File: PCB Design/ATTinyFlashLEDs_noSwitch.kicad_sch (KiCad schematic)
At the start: 11 parts, among them J1 Conn_01x04_Pin, J2 Conn_01x04_Pin, J3 Conn_01x03_Pin, U1 ATtiny85V-10P

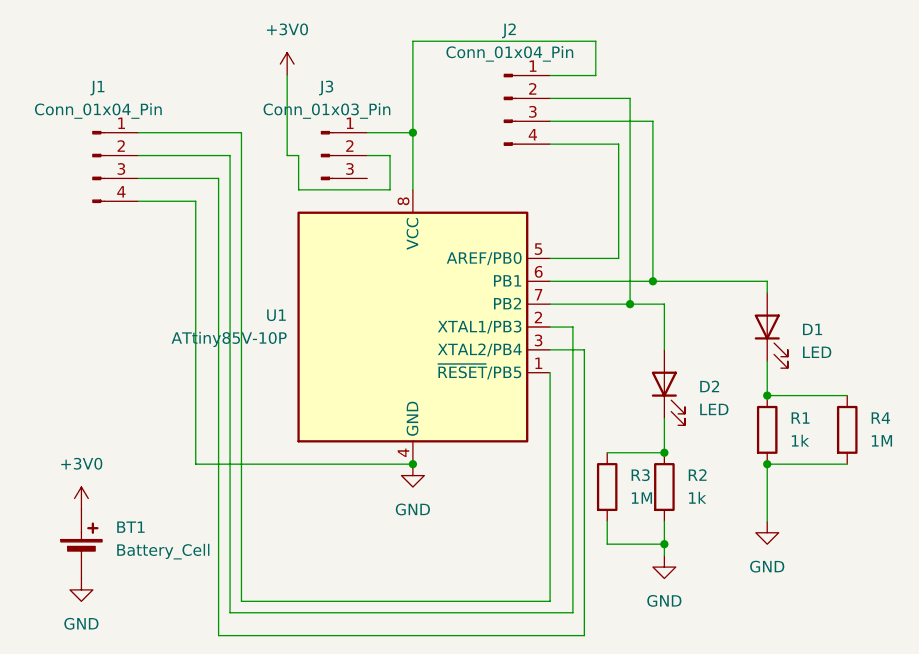
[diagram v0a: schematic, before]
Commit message: Added decoupling capacitor, moved power trace to back copper
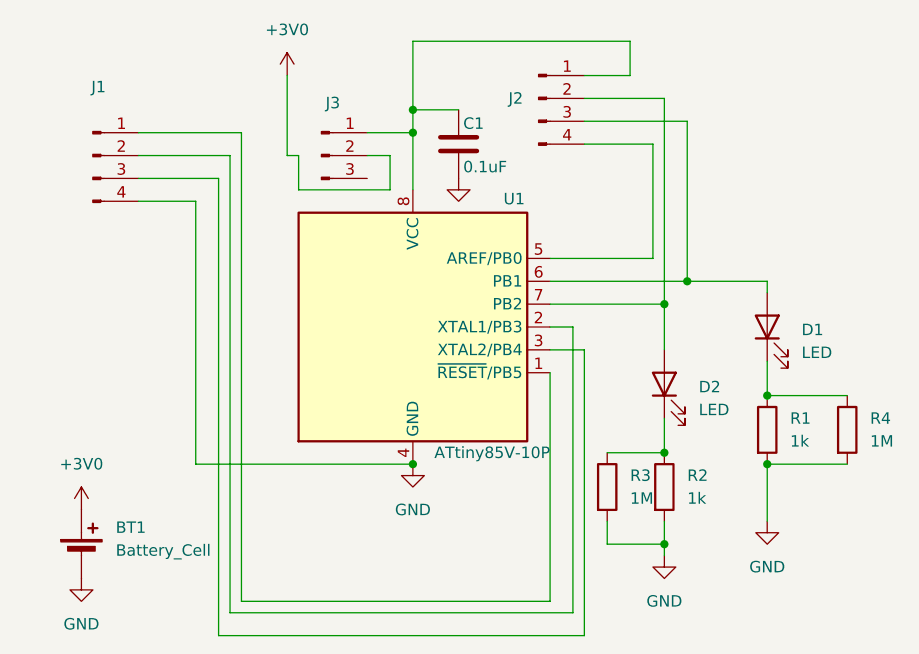
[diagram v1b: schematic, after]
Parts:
- added C1: 0.1uF, Capacitor_SMD:C_0603_1608Metric_Pad1.08x0.95mm_HandSolder, symbol Device:C
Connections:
- net GND: now also C1.2
- net at J2.1 (Pin_1), J3.1 (Pin_1), U1.8 (VCC): now also C1.1
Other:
- moved on the sheet: J2
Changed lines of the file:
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@@
 	)
 	(junction
-		(at 83.82 43.18)
+		(at 85.09 45.72)
+		(diameter 0)
+		(color 0 0 0 0)
+	)
+	(junction
+		(at 57.15 24.13)
 		(diameter 0)
 		(color 0 0 0 0)
@@
 	)
 	(junction
-		(at 81.28 45.72)
+		(at 57.15 26.67)
 		(diameter 0)
 		(color 0 0 0 0)
 	)
 	(junction
-		(at 57.15 26.67)
+		(at 87.63 43.18)
 		(diameter 0)
 		(color 0 0 0 0)
@@
 	(wire
 		(pts
-			(xy 81.28 22.86) (xy 81.28 45.72)
+			(xy 57.15 24.13) (xy 62.23 24.13)
+		)
+		(stroke
+			(width 0)
+			(type default)
+		)
+	)
+	(wire
+		(pts
+			(xy 85.09 22.86) (xy 85.09 45.72)
 		)
 		(stroke
@@
 	(wire
 		(pts
-			(xy 72.39 25.4) (xy 83.82 25.4)
+			(xy 76.2 25.4) (xy 87.63 25.4)
 		)
 		(stroke
@@
 	(wire
 		(pts
-			(xy 83.82 43.18) (xy 96.52 43.18)
-		)
-		(stroke
-			(width 0)
-			(type default)
-		)
-	)
-	(wire
-		(pts
-			(xy 81.28 45.72) (xy 85.09 45.72)
-		)
-		(stroke
-			(width 0)
-			(type default)
-		)
-	)
-	(wire
-		(pts
 			(xy 26.67 34.29) (xy 33.02 34.29)
 		)
@@
 	(wire
 		(pts
-			(xy 83.82 25.4) (xy 83.82 43.18)
+			(xy 87.63 25.4) (xy 87.63 43.18)
 		)
 		(stroke
@@
 	(wire
 		(pts
-			(xy 72.39 27.94) (xy 80.01 27.94)
+			(xy 76.2 27.94) (xy 83.82 27.94)
 		)
 		(stroke
@@
 	(wire
 		(pts
-			(xy 72.39 20.32) (xy 77.47 20.32)
-		)
-		(stroke
-			(width 0)
-			(type default)
-		)
-	)
-	(wire
-		(pts
-			(xy 77.47 16.51) (xy 57.15 16.51)
+			(xy 76.2 20.32) (xy 81.28 20.32)
+		)
+		(stroke
+			(width 0)
+			(type default)
+		)
+	)
+	(wire
+		(pts
+			(xy 57.15 24.13) (xy 57.15 26.67)
+		)
+		(stroke
+			(width 0)
+			(type default)
+		)
+	)
+	(wire
+		(pts
+			(xy 81.28 16.51) (xy 57.15 16.51)
 		)
 		(stroke
@@
 	(wire
 		(pts
-			(xy 72.39 40.64) (xy 80.01 40.64)
-		)
-		(stroke
-			(width 0)
-			(type default)
-		)
-	)
-	(wire
-		(pts
-			(xy 72.39 43.18) (xy 83.82 43.18)
+			(xy 72.39 40.64) (xy 83.82 40.64)
+		)
+		(stroke
+			(width 0)
+			(type default)
+		)
+	)
+	(wire
+		(pts
+			(xy 87.63 43.18) (xy 96.52 43.18)
+		)
+		(stroke
+			(width 0)
+			(type default)
+		)
+	)
+	(wire
+		(pts
+			(xy 72.39 43.18) (xy 87.63 43.18)
 		)
 		(stroke
@@
 	(wire
 		(pts
-			(xy 72.39 22.86) (xy 81.28 22.86)
+			(xy 76.2 22.86) (xy 85.09 22.86)
 		)
 		(stroke
@@
 	(wire
 		(pts
-			(xy 80.01 40.64) (xy 80.01 27.94)
-		)
-		(stroke
-			(width 0)
-			(type default)
-		)
-	)
-	(wire
-		(pts
-			(xy 57.15 16.51) (xy 57.15 26.67)
-		)
-		(stroke
-			(width 0)
-			(type default)
-		)
-	)
-	(wire
-		(pts
-			(xy 72.39 45.72) (xy 81.28 45.72)
+			(xy 83.82 40.64) (xy 83.82 27.94)
+		)
+		(stroke
+			(width 0)
+			(type default)
+		)
+	)
+	(wire
+		(pts
+			(xy 57.15 16.51) (xy 57.15 24.13)
+		)
+		(stroke
+			(width 0)
+			(type default)
+		)
+	)
+	(wire
+		(pts
+			(xy 72.39 45.72) (xy 85.09 45.72)
 		)
 		(stroke
@@
 	(wire
 		(pts
-			(xy 77.47 20.32) (xy 77.47 16.51)
+			(xy 81.28 20.32) (xy 81.28 16.51)
 		)
 		(stroke
@@
 	(symbol
 		(lib_id "Connector:Conn_01x04_Pin")
-		(at 67.31 22.86 0)
+		(at 71.12 22.86 0)
 		(unit 1)
 		(exclude_from_sim no)
@@
 		(on_board yes)
 		(dnp no)
-		(fields_autoplaced yes)
 		(property "Reference" "J2"
-			(at 67.945 15.24 0)
+			(at 68.58 22.86 0)
 			(effects
 				(font
@@
 		)
 		(property "Value" "Conn_01x04_Pin"
-			(at 67.945 17.78 0)
-			(effects
-				(font
-					(size 1.27 1.27)
-				)
+			(at 71.755 17.78 0)
+			(effects
+				(font
+					(size 1.27 1.27)
+				)
+				(hide yes)
 			)
 		)
 		(property "Footprint" "Connector_PinHeader_2.54mm:PinHeader_1x04_P2.54mm_Vertical"
-			(at 67.31 22.86 0)
+			(at 71.12 22.86 0)
 			(effects
 				(font
@@
 		)
 		(property "Datasheet" "~"
-			(at 67.31 22.86 0)
+			(at 71.12 22.86 0)
 			(effects
 				(font
@@
 		)
 		(property "Description" "Generic connector, single row, 01x04, script generated"
-			(at 67.31 22.86 0)
+			(at 71.12 22.86 0)
 			(effects
 				(font
@@
 	)
 	(symbol
+		(lib_id "Device:C")
+		(at 62.23 27.94 0)
+		(unit 1)
+		(exclude_from_sim no)
+		(in_bom yes)
+		(on_board yes)
+		(dnp no)
+		(property "Reference" "C1"
+			(at 62.738 25.654 0)
+			(effects
+				(font
+					(size 1.27 1.27)
+				)
+				(justify left)
+			)
+		)
+		(property "Value" "0.1uF"
+			(at 62.738 30.48 0)
+			(effects
+				(font
+					(size 1.27 1.27)
+				)
+				(justify left)
+			)
+		)
+		(property "Footprint" "Capacitor_SMD:C_0603_1608Metric_Pad1.08x0.95mm_HandSolder"
+			(at 63.1952 31.75 0)
+			(effects
+				(font
+					(size 1.27 1.27)
+				)
+				(hide yes)
+			)
+		)
+		(property "Datasheet" "~"
+			(at 62.23 27.94 0)
+			(effects
+				(font
+					(size 1.27 1.27)
+				)
+				(hide yes)
+			)
+		)
+		(property "Description" "Unpolarized capacitor"
+			(at 62.23 27.94 0)
+			(effects
+				(font
+					(size 1.27 1.27)
+				)
+				(hide yes)
+			)
+		)
+		(pin "2"
+		)
+		(pin "1"
+		)
+		(instances
+			(project ""
+				(path "/3e34162c-5c2f-4b82-8cf2-6b7148cf69da"
+					(reference "C1")
+					(unit 1)
+				)
+			)
+		)
+	)
+	(symbol
 		(lib_id "Device:Battery_Cell")
 		(at 20.32 73.66 0)
@@
 		(on_board yes)
 		(dnp no)
-		(fields_autoplaced yes)
 		(property "Reference" "J3"
-			(at 47.625 21.59 0)
+			(at 48.26 23.368 0)
 			(effects
 				(font
@@
 					(size 1.27 1.27)
 				)
+				(hide yes)
 			)
 		)
@@
 		(on_board yes)
 		(dnp no)
-		(fields_autoplaced yes)
 		(property "Reference" "J1"
 			(at 22.225 21.59 0)
@@
 		)
 		(property "Value" "Conn_01x04_Pin"
-			(at 22.225 24.13 0)
-			(effects
-				(font
-					(size 1.27 1.27)
-				)
+			(at 22.352 24.638 0)
+			(effects
+				(font
+					(size 1.27 1.27)
+				)
+				(hide yes)
 			)
 		)
@@
 		(on_board yes)
 		(dnp no)
-		(fields_autoplaced yes)
 		(property "Reference" "U1"
-			(at 43.18 46.9899 0)
+			(at 69.596 34.036 0)
 			(effects
 				(font
@@
 		)
 		(property "Value" "ATtiny85V-10P"
-			(at 43.18 49.5299 0)
+			(at 72.39 62.23 0)
 			(effects
 				(font
@@
 					(unit 1)
 				)
+			)
+		)
+	)
+	(symbol
+		(lib_id "power:GND")
+		(at 62.23 31.75 0)
+		(unit 1)
+		(exclude_from_sim no)
+		(in_bom yes)
+		(on_board yes)
+		(dnp no)
+		(fields_autoplaced yes)
+		(property "Reference" "#PWR07"
+			(at 62.23 38.1 0)
+			(effects
+				(font
+					(size 1.27 1.27)
+				)
+				(hide yes)
+			)
+		)
+		(property "Value" "GND"
+			(at 62.23 36.83 0)
+			(effects
+				(font
+					(size 1.27 1.27)
+				)
+				(hide yes)
+			)
+		)
+		(property "Footprint" ""
+			(at 62.23 31.75 0)
+			(effects
+				(font
+					(size 1.27 1.27)
+				)
+				(hide yes)
+			)
+		)
+		(property "Datasheet" ""
+			(at 62.23 31.75 0)
+			(effects
+				(font
+					(size 1.27 1.27)
+				)
+				(hide yes)
+			)
+		)
+		(property "Description" "Power symbol creates a global label with name \"GND\" , ground"
+			(at 62.23 31.75 0)
+			(effects
+				(font
+					(size 1.27 1.27)
+				)
+				(hide yes)
+			)
+		)
+		(pin "1"
+		)
+		(instances
+			(project "ATTinyFlashLEDs_noSwitch"
+				(path "/3e34162c-5c2f-4b82-8cf2-6b7148cf69da"
+					(reference "#PWR07")
+					(unit 1)
+				)
